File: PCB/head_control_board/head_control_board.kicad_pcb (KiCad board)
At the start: 2 copper layers, 104.5 x 72.5 mm, 60 parts, among them Q1 AO3401A, U1 TPS63070RNMR, U2 TPS63070RNMR, U3 SN74AHCT245PWR, U4 ESP32-S3-WROOM-1(N16R8)

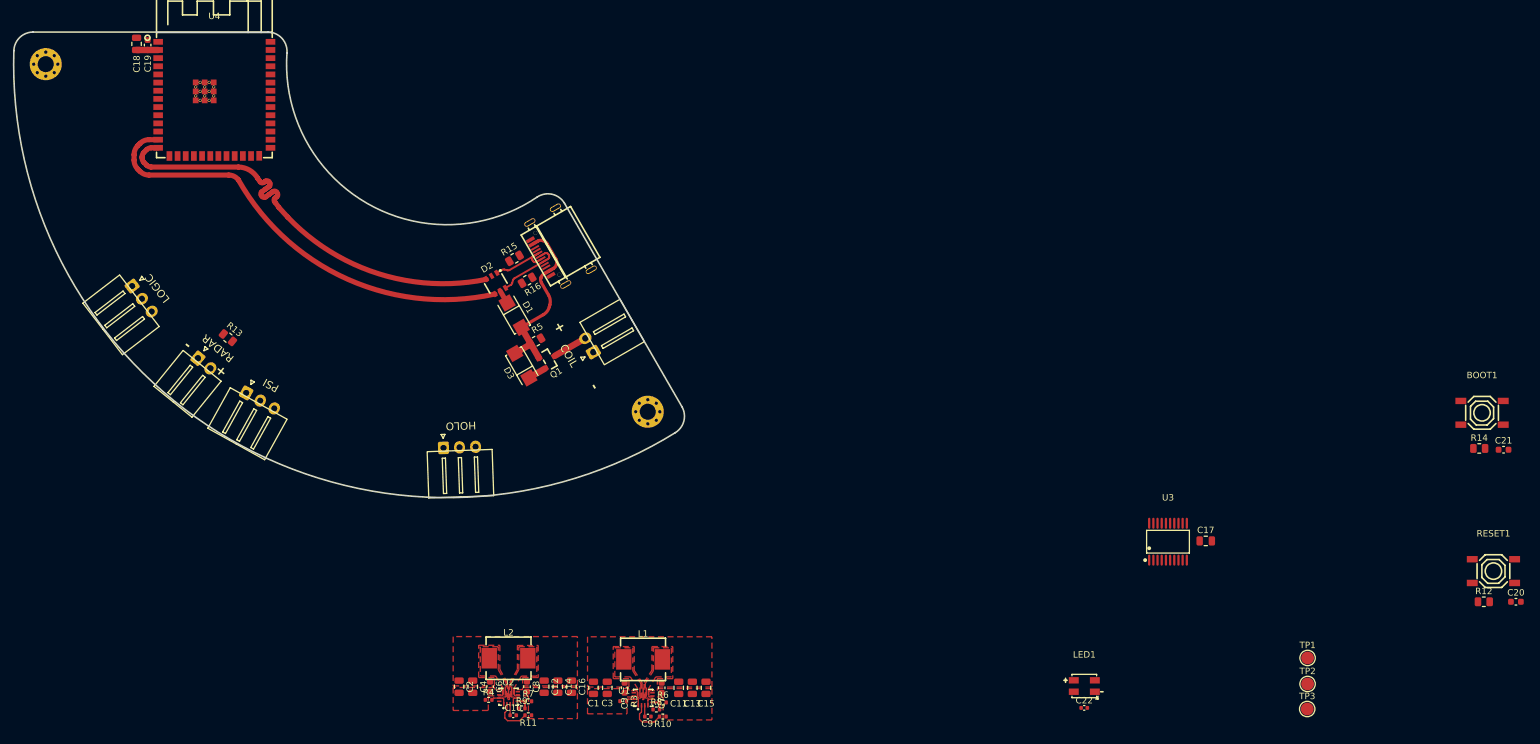
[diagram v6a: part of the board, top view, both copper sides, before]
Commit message: Finish signal routing
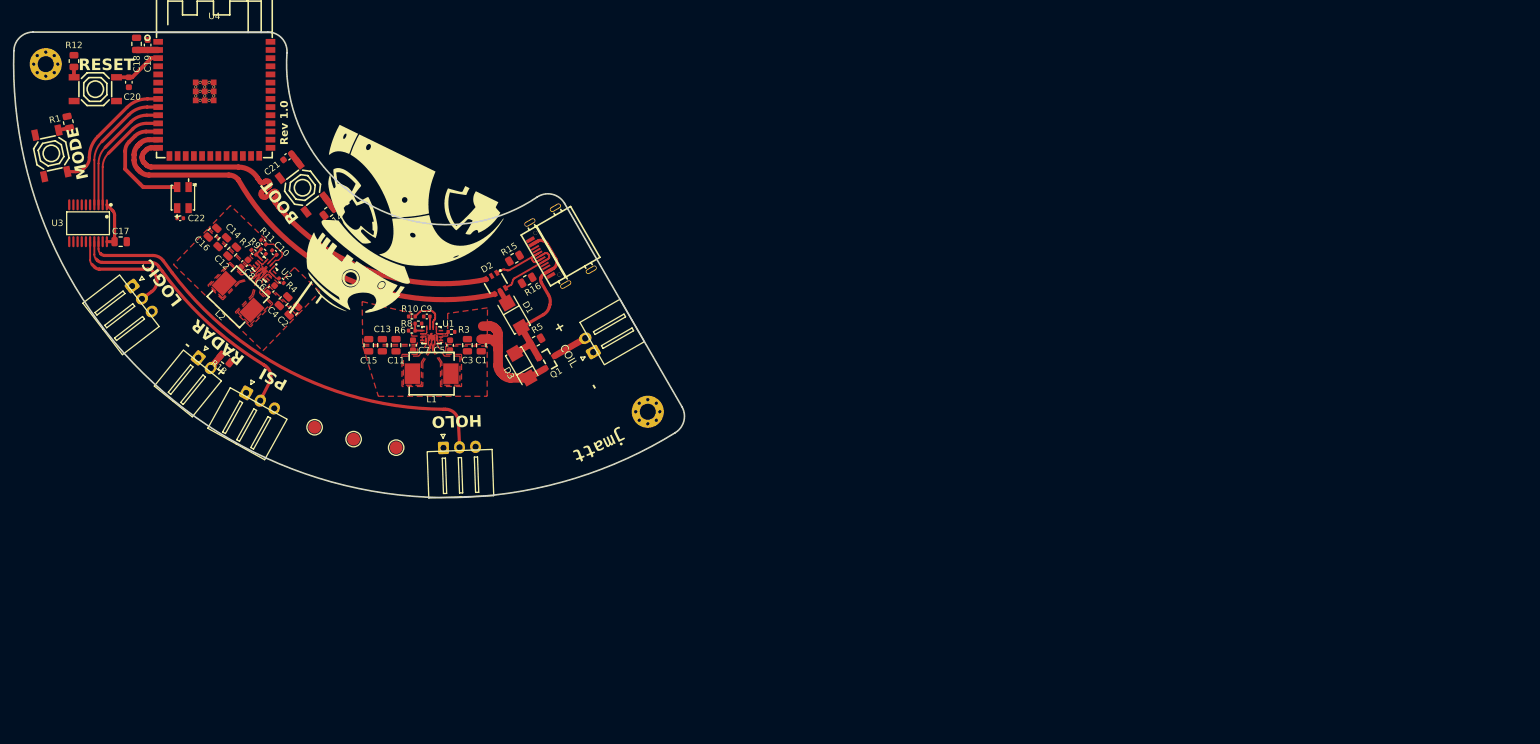
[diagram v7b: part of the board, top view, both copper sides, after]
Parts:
- added G***: LOGO, LOGO, F.Cu at (111.2, 94.9)
- added G***: LOGO, LOGO, F.Cu at (83.7, 65.3)
- added R1: 10k, Resistor_SMD:R_0805_2012Metric, F.Cu at (34.9, 45.2)
- added SELECT1: TS-1187A-B-A-B, LCSC:SW-SMD_4P-L5.1-W5.1-P3.70-LS6.5-TL-2, F.Cu at (32.3, 50.1)
- moved R12 235.1 mm to (35.8, 35.7), turned to -90 degrees
- moved C20 230.7 mm to (44.4, 39.0), turned to 90 degrees
- moved RESET1 230.3 mm to (39.1, 40.1)
- moved C21 194.8 mm to (69.1, 50.6), turned to -142.5 degrees
- moved BOOT1 187.0 mm to (71.4, 55.4), turned to -52.5 degrees
- moved R14 182.9 mm to (75.5, 59.2), turned to -142.5 degrees
- moved U3 175.3 mm to (38.0, 61.0), turned to 180 degrees
- moved C17 175.3 mm to (43.1, 63.8), turned to 180 degrees
- moved C22 160.1 mm to (52.4, 60.2)
- moved TP2 159.7 mm to (73.3, 92.7), turned to 90 degrees
- moved LED1 159.7 mm to (52.8, 57.0), turned to 90 degrees
- moved TP1 152.4 mm to (79.3, 94.6), turned to 90 degrees
- moved TP3 147.6 mm to (86.0, 95.9), turned to 90 degrees
- moved C16 90.1 mm to (57.4, 62.4), turned to 46 degrees
- moved C14 86.7 mm to (58.9, 63.9), turned to 46 degrees
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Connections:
- C22 pad 1: GND -> +3.3V
- C22 pad 2: +3.3V -> GND
- U4 pad 10: /LED3_3V3 -> /LED2_3V3
- U4 pad 11: /LED2_3V3 -> /LED1_3V3
- U4 pad 12: /LED1_3V3 -> Net-(LED1-DIN)
- U4 pad 39: Net-(LED1-DIN) -> unconnected-(U4-IO1-Pad39)
- U4 pad 8: unconnected-(U4-IO15-Pad8) -> /SELECT
- U4 pad 9: unconnected-(U4-IO16-Pad9) -> /LED3_3V3
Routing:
- net /LED1_5V: track 0.00 -> 70.2 mm
- net /LED2_5V: track 0.00 -> 41.7 mm
- net /LED3_3V3: track 0.00 -> 20.9 mm
- net /SELECT: track 0.00 -> 19.8 mm
- net /LED2_3V3: track 0.00 -> 19.3 mm
- net /LED3_5V: track 0.00 -> 18.9 mm
- net Net-(LED1-DIN): track 0.00 -> 18.7 mm
- net /LED1_3V3: track 0.00 -> 17.8 mm
- net +VIN: track 2.90 -> 20.6 mm
- net +5V: track 0.00 -> 7.89 mm
- net Net-(RESET1-B): track 0.00 -> 7.72 mm
- net Net-(RADAR1-Pin_2): track 0.00 -> 2.55 mm
- net Net-(BOOT1-B): track 0.00 -> 2.15 mm
- net Net-(BOOT1-A): track 0.00 -> 1.95 mm
- net Net-(SELECT1-A): track 0.00 -> 1.74 mm
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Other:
- board text added: "BOOT"
- board text added: "MODE"
- board text added: "RESET"
- board text added: "Rev 1.0"

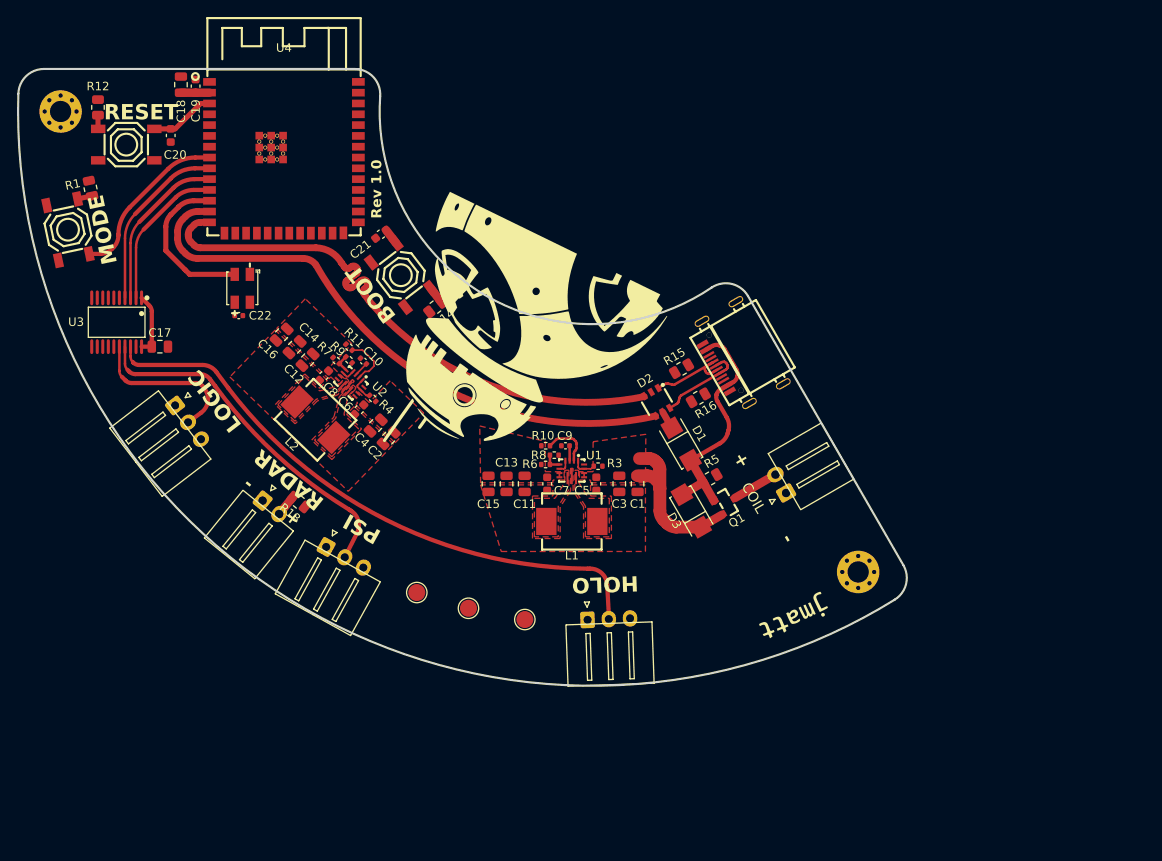
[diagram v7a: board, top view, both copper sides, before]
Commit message: Finish power routing
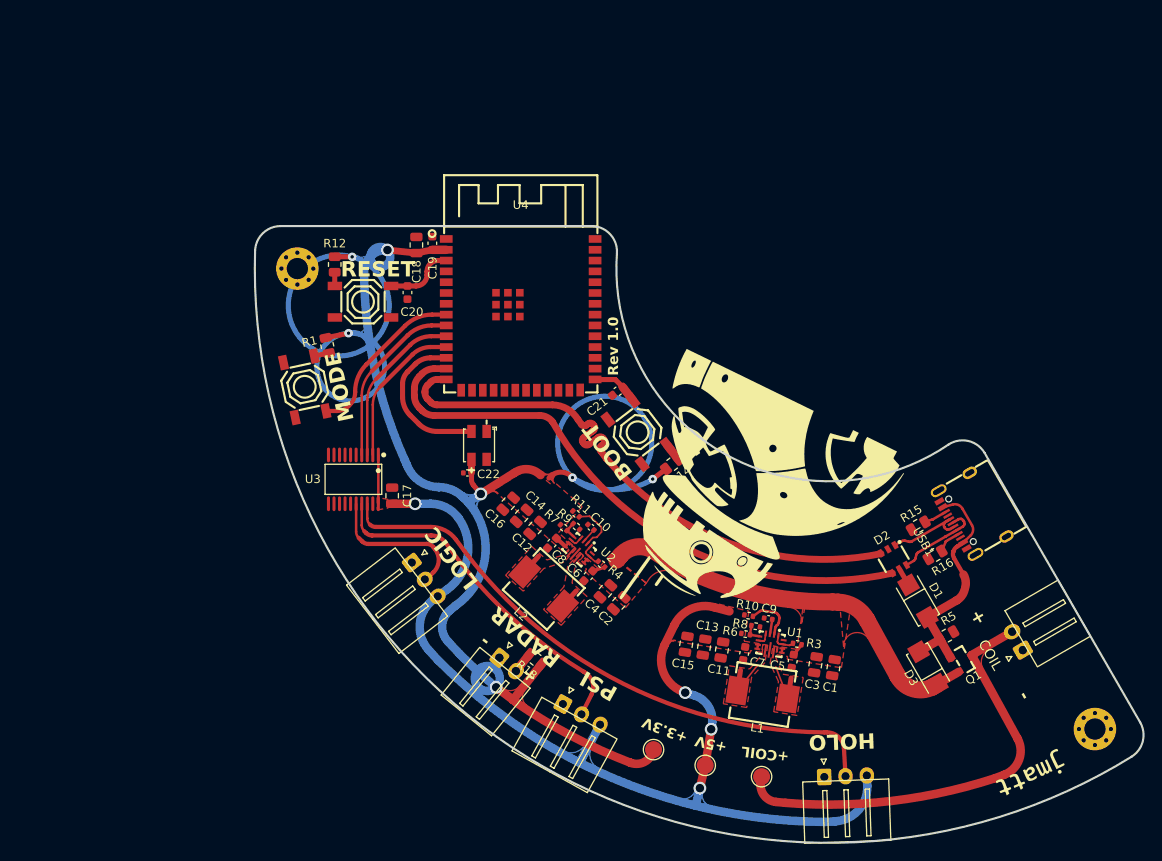
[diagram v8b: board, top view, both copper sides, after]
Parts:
- removed USBC1: TYPE-C-31-M-14, LCSC:USB-C-SMD_12P-P0.50-H-F_TYPE-C-31-M-14
- added USB1: TYPE-C 16PIN 2MD(073), LCSC:USB-C-SMD_TYPE-C-6PIN-2MD-073, F.Cu at (138.4, 83.6)
- moved C18 33.5 mm to (73.2, 51.9)
- moved L2 33.4 mm to (88.2, 92.3), turned to 138 degrees
- moved LOGIC1 33.4 mm to (72.7, 89.2)
- moved TP2 33.4 mm to (101.1, 111.2)
- moved C20 33.4 mm to (72.2, 57.5)
- moved COIL1 33.4 mm to (144.5, 99.5)
- moved R12 33.4 mm to (63.6, 54.2)
- moved BOOT1 33.4 mm to (99.2, 73.9)
- moved C21 33.4 mm to (96.9, 69.1)
- moved R16 33.4 mm to (134.2, 88.3)
- moved U4 33.4 mm to (85.5, 60.1)
- moved G*** 33.4 mm to (111.6, 83.8)
- moved R13 33.4 mm to (87.2, 100.6)
- moved R15 33.4 mm to (132.2, 84.9)
- moved TP1 33.4 mm to (107.2, 113.0)
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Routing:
- net +3.3V: track 3.36 -> 167.0 mm, vias 0 -> 7
- net +5V: track 7.89 -> 129.6 mm, vias 0 -> 4
- net +VCOIL: track 5.50 -> 52.7 mm
- net +VIN: track 20.6 -> 51.5 mm
- net Net-(U1-L1): track 0.00 -> 6.43 mm
- net Net-(U1-L2): track 0.00 -> 6.06 mm
- net Net-(BOOT1-A): track 1.95 -> 5.60 mm
- net /USB-D+: track 65.5 -> 69.0 mm
- net Net-(USB1-CC1): track 0.00 -> 2.93 mm
- net Net-(USB1-CC2): track 0.00 -> 2.70 mm
- net Net-(U2-L2): track 0.00 -> 2.43 mm
- net Net-(U2-L1): track 0.00 -> 2.40 mm
- net /USB-D-: track 67.9 -> 69.6 mm
- net /LED3_5V: track 18.9 -> 17.8 mm
- net /D+: track 10.5 -> 9.93 mm
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- added copper zone on B.Cu, net +3.3V
- added copper zone on B.Cu, net +5V
- added copper zone on F.Cu, net +VCOIL
- removed copper zone on F.Cu, net GND
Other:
- board text added: "+3.3V"
- board text added: "+5V"
- board text added: "+COIL"
- board text removed: "${REFERENCE}"
